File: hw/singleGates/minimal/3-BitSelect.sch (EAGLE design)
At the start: 36 parts, among them Q1 BC817, Q10 BC817, Q11 BC817, Q12 BC817, Q13 BC817, Q14 BC817, Q15 BC817, Q16 BC817, Q17 BC817, Q2 BC817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

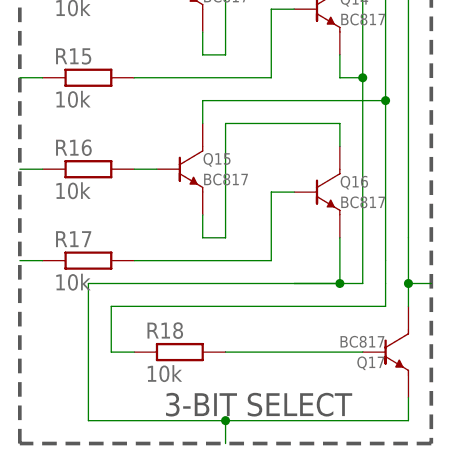
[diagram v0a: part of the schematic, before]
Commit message: fixes some offset and juction issues
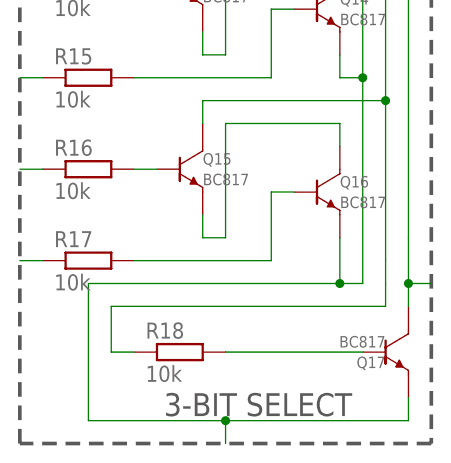
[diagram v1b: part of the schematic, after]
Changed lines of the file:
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@@
 <wire x1="0" y1="-91.44" x2="-15.24" y2="-91.44" width="0.1524" layer="91"/>
 <wire x1="-15.24" y1="-91.44" x2="-15.24" y2="-76.2" width="0.1524" layer="91"/>
-<wire x1="-15.24" y1="-76.2" x2="7.62" y2="-76.2" width="0.1524" layer="91"/>
-<wire x1="7.62" y1="-76.2" x2="12.7" y2="-76.2" width="0.1524" layer="91"/>
+<wire x1="-15.24" y1="-76.2" x2="12.7" y2="-76.2" width="0.1524" layer="91"/>
 <wire x1="12.7" y1="-76.2" x2="12.7" y2="-71.12" width="0.1524" layer="91"/>
 <wire x1="15.24" y1="-53.34" x2="15.24" y2="-76.2" width="0.1524" layer="91"/>
 <wire x1="15.24" y1="-76.2" x2="12.7" y2="-76.2" width="0.1524" layer="91"/>
-<wire x1="12.7" y1="-76.2" x2="7.62" y2="-76.2" width="0.1524" layer="91"/>
 <wire x1="20.32" y1="-88.9" x2="20.32" y2="-91.44" width="0.1524" layer="91"/>
 <pinref part="Q17" gate="G$1" pin="EMITTER"/>

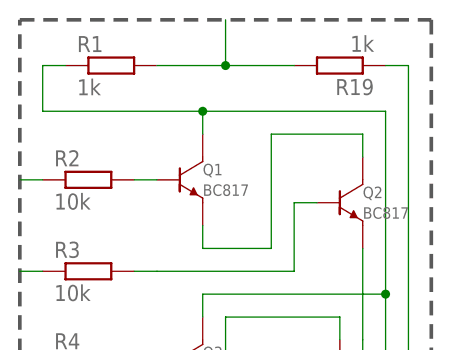
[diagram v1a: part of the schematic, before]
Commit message: Add led output and prepare first alu slice
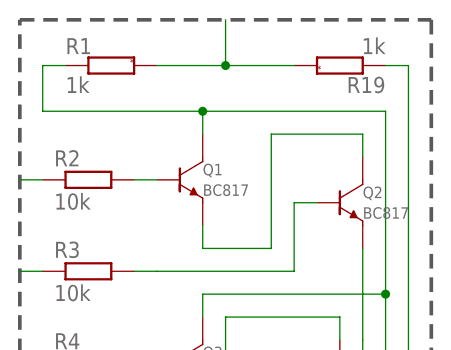
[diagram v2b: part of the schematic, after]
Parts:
- R1, R19: device p.peter-gator:R-EU_R0603 -> p.peter-rcl:R-EU-MARKEDR0603
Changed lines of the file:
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@@
 <part name="R2" library="p.peter-gator" deviceset="R-EU_" device="R0603" value="10k"/>
 <part name="R3" library="p.peter-gator" deviceset="R-EU_" device="R0603" value="10k"/>
-<part name="R1" library="p.peter-gator" deviceset="R-EU_" device="R0603" value="1k"/>
+<part name="R1" library="p.peter-rcl" deviceset="R-EU-MARKED" device="R0603" value="1k"/>
 <part name="R4" library="p.peter-gator" deviceset="R-EU_" device="R0603" value="10k"/>
 <part name="R5" library="p.peter-gator" deviceset="R-EU_" device="R0603" value="10k"/>
@@
 <part name="R17" library="p.peter-gator" deviceset="R-EU_" device="R0603" value="10k"/>
 <part name="R18" library="p.peter-gator" deviceset="R-EU_" device="R0603" value="10k"/>
-<part name="R19" library="p.peter-gator" deviceset="R-EU_" device="R0603" value="1k"/>
+<part name="R19" library="p.peter-rcl" deviceset="R-EU-MARKED" device="R0603" value="1k"/>
 <part name="Q1" library="p.peter-gator" deviceset="TRANSISTOR-NPN-GENERIC" device="-SOT23-BEC" technology="DEFAULT" value="BC817"/>
 <part name="Q2" library="p.peter-gator" deviceset="TRANSISTOR-NPN-GENERIC" device="-SOT23-BEC" technology="DEFAULT" value="BC817"/>
